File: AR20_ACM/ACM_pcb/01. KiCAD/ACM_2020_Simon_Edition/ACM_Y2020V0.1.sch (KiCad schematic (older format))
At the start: 31 parts, among them J1 TC2030-MCP-NL, P1 Conn_02x15_Odd_Even, Q1 Q_PMOS_DGS, U2 MCP25625-x-SS, U3 NCV890430MW50TXG, Y1 16.0Mhz

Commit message: AtmegaFix
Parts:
- added U?: ATmega328P-AU, Package_QFP:TQFP-32_7x7mm_P0.8mm, symbol MCU_Microchip_ATmega:ATmega328P-AU
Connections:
- wire segments 105 -> 109
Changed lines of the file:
@@
 EESchema Schematic File Version 4
 LIBS:ACM_Y2020V0.1-cache
-EELAYER 30 0
+EELAYER 29 0
 EELAYER END
 $Descr A4 11693 8268
@@
 Text HLabel 6600 2275 2    50   Input ~ 0
 U-Pin24
-Text Notes 3425 6225 0    50   ~ 0
+Text Notes 3275 6225 0    50   ~ 0
 Legg ut RESET for Debugwire
 $Comp
@@
 AVCC Lavpass filter
 Wire Wire Line
-	2850 4125 2700 4125
-Connection ~ 2700 4125
-Wire Wire Line
-	2700 4125 2600 4125
-Wire Wire Line
-	2400 4125 2175 4125
-Connection ~ 2175 4125
+	2400 4125 2275 4125
 Text Notes 1150 4600 2    50   ~ 0
 Place as close as \npossible to pin 20
@@
 Text Notes 9625 875  0    50   ~ 0
 RGB krets\n
+Wire Wire Line
+	2600 4125 2850 4125
+$Comp
+L MCU_Microchip_ATmega:ATmega328P-AU U?
+U 1 1 5DD5CA89
+P 2175 5775
+F 0 "U?" H 2175 4186 50  0000 C CNN
+F 1 "ATmega328P-AU" H 2175 4095 50  0000 C CNN
+F 2 "Package_QFP:TQFP-32_7x7mm_P0.8mm" H 2175 5775 50  0001 C CIN
+F 3 "http://ww1.microchip.com/downloads/en/DeviceDoc/ATmega328_P%20AVR%20MCU%20with%20picoPower%20Technology%20Data%20Sheet%2040001984A.pdf" H 2175 5775 50  0001 C CNN
+	1    2175 5775
+	1    0    0    -1
+$EndComp
+Wire Wire Line
+	2175 4275 2175 4125
+Connection ~ 2175 4125
+Wire Wire Line
+	2275 4275 2275 4125
+Connection ~ 2275 4125
+Wire Wire Line
+	2275 4125 2175 4125
+Wire Wire Line
+	1300 4625 1300 4575
+Wire Wire Line
+	1300 4575 1575 4575
 $EndSCHEMATC

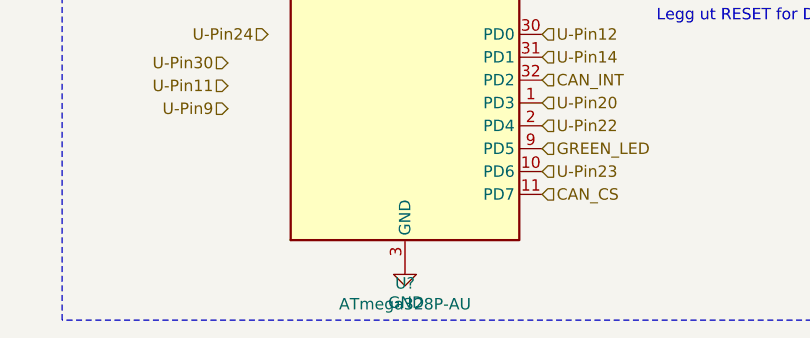
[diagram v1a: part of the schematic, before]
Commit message: Exploded and connected MCP25625 RX and TX 2
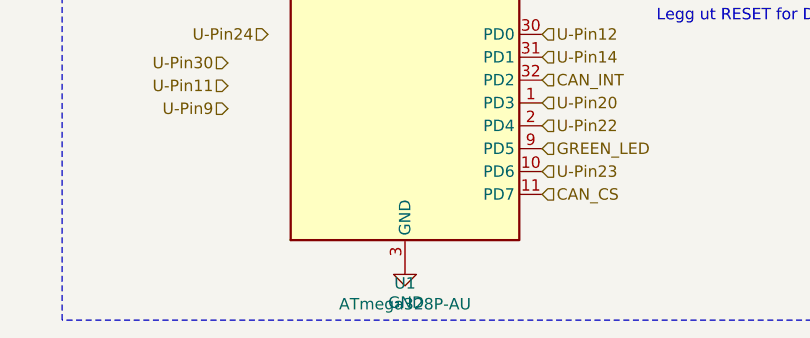
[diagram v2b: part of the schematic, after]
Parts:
- gave numbers to parts that had none: 1
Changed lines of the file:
@@
 	9625 1725 9525 1725
 $Comp
-L power:+5V #PWR?
+L power:+5V #PWR0103
 U 1 1 5DDBB889
 P 10100 1475
-F 0 "#PWR?" H 10100 1325 50  0001 C CNN
+F 0 "#PWR0103" H 10100 1325 50  0001 C CNN
 F 1 "+5V" H 10115 1648 50  0000 C CNN
 F 2 "" H 10100 1475 50  0001 C CNN
@@
 	2600 4125 2850 4125
 $Comp
-L MCU_Microchip_ATmega:ATmega328P-AU U?
+L MCU_Microchip_ATmega:ATmega328P-AU U1
 U 1 1 5DD5CA89
 P 2175 5775
-F 0 "U?" H 2175 4186 50  0000 C CNN
+F 0 "U1" H 2175 4186 50  0000 C CNN
 F 1 "ATmega328P-AU" H 2175 4095 50  0000 C CNN
 F 2 "Package_QFP:TQFP-32_7x7mm_P0.8mm" H 2175 5775 50  0001 C CIN
